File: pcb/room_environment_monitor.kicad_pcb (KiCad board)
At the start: 4 copper layers, 35.5 x 74.7 mm, 54 parts, among them J1 Conn_01x02_Pin, J2 Conn_01x04_Pin, J3 Conn_01x06_Socket, P1 USB_C_Plug_USB2.0, Q1 BSS138, Q3 BSS138, SW1 SW_SPST, U2 ESP32-C3-MINI-1, U3 SGP30-2.5K, U4 BME280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

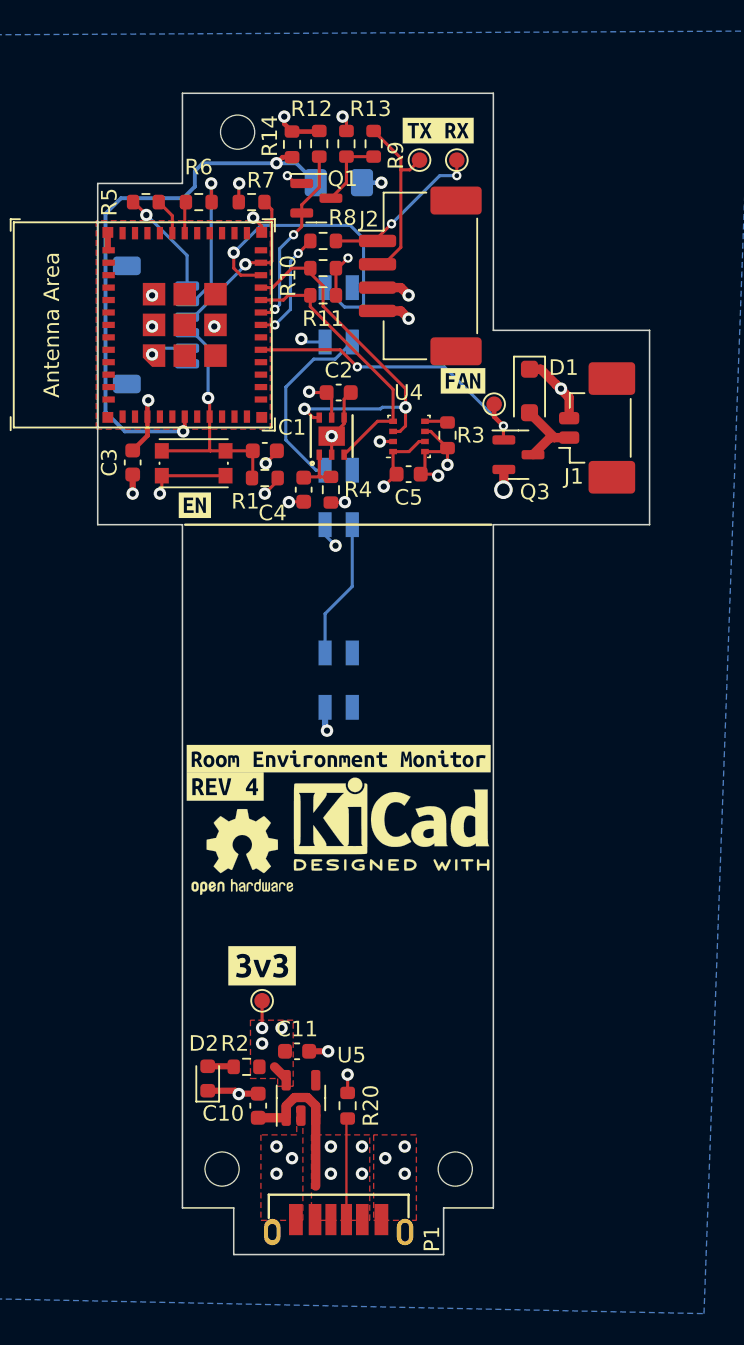
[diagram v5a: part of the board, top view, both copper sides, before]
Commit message: cleanup undeeded pdf files and add gerbers
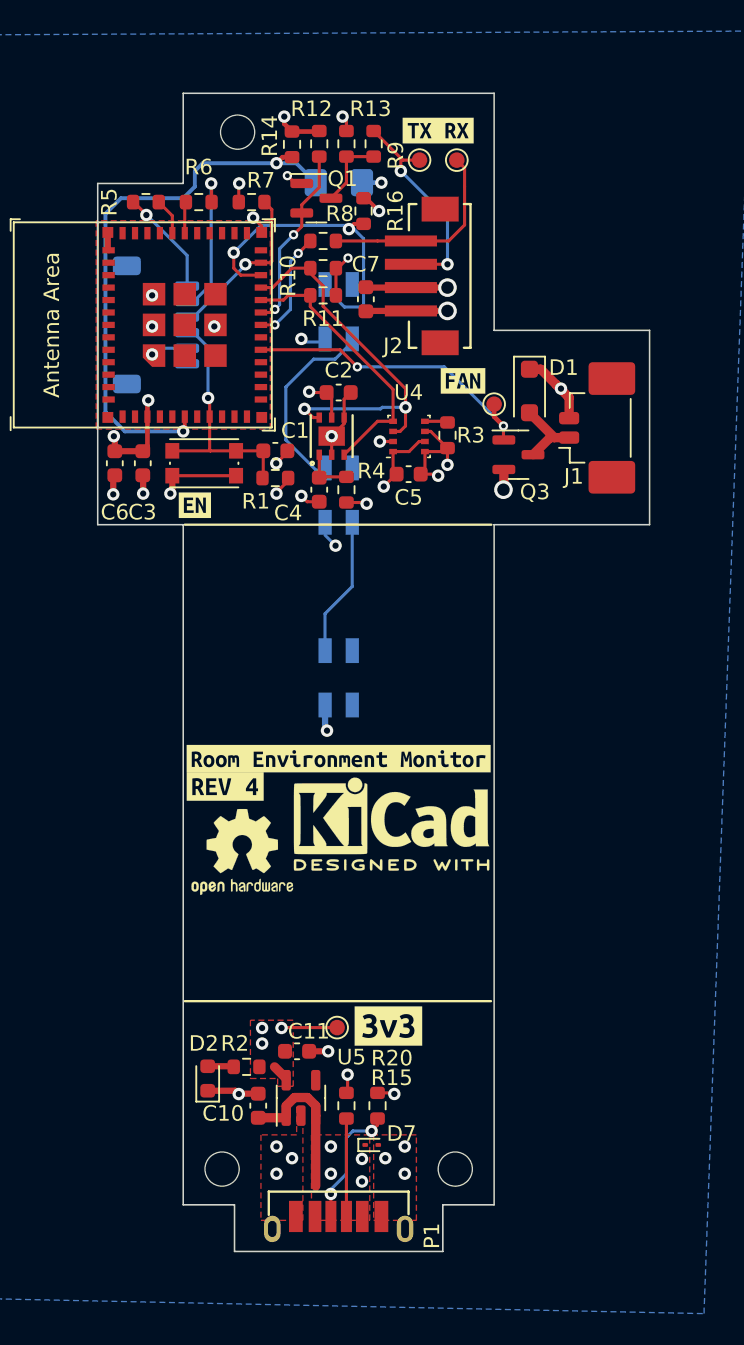
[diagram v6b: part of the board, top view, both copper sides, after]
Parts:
- added C6: 1u, Capacitor_SMD:C_0603_1608Metric, F.Cu at (95.6, 93.8)
- added C7: 1u, Capacitor_SMD:C_0603_1608Metric, F.Cu at (111.8, 83.2)
- added D7: ESD9X3, Diode_SMD:D_SOD-923, F.Cu at (112.1, 137.7)
- added R15: 5.1k, Resistor_SMD:R_0603_1608Metric, F.Cu at (112.5, 135.1)
- added R16: 10k, Resistor_SMD:R_0603_1608Metric, F.Cu at (111.6, 77.6)
- J2: footprint Connector_JST:JST_ZE_BM04B-ZESS-TBT_1x04-1MP_P1.50mm_Vertical -> Kevin_Lutzer_Lbr:CONN_B4B-ZR-SM4-TF_JST
- moved kibuzzard-652F0EDE 9.00 mm to (113.2, 130.0)
- moved TP4 5.12 mm to (109.9, 130.1)
- moved J2 1.25 mm to (116.5, 81.8)
- moved C4 1.00 mm to (108.8, 95.5)
- moved R4 1.00 mm to (110.5, 95.5)
- moved C1 0.67 mm to (105.9, 93.0)
- moved R1 0.67 mm to (105.9, 94.8)
- moved SW1 0.67 mm to (101.3, 93.8)
- moved C3 0.65 mm to (97.4, 93.8)
- moved D3 0.20 mm to (110.0, 84.0)
- moved P1 0.20 mm to (110.0, 143.1)
- moved D4 0.15 mm to (110.0, 95.8)
- moved D5 0.15 mm to (110.0, 107.6)
- moved R20 0.08 mm to (110.5, 135.1)
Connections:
- net CC renamed Net-(P1-CC)
- P1 pad B5: unconnected-(P1-VCONN-PadB5) -> Net-(P1-VCONN)
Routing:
- net Net-(P1-VCONN): track 0.00 -> 8.25 mm, vias 0 -> 2
- net Net-(P1-CC): track 6.53 -> 12.8 mm
- net +3V3: track 26.3 -> 32.4 mm, vias 14 -> 16
- net GND: track 37.1 -> 42.9 mm, vias 26 -> 28
- net +5V: track 17.9 -> 20.9 mm
- net Net-(J2-Pin_2): track 11.1 -> 14.1 mm, vias 0 -> 2
- net Net-(J2-Pin_1): track 10.4 -> 13.1 mm, vias 2 -> 0
- net NEOPIXEL: track 19.7 -> 20.7 mm, vias 1 -> 2
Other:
- board size 35.5 x 74.7 mm -> 35.5 x 74.5 mm

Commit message: update fab
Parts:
- C10: value 10u -> 1u
- C11: value 22u -> 1u
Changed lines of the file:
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@@
         (effects (font (size 1 1) (thickness 0.15)))
     )
-    (fp_text value "22u" (at 0 1.43) (layer "F.Fab")
+    (fp_text value "1u" (at 0 1.43) (layer "F.Fab")
         (effects (font (size 1 1) (thickness 0.15)))
     )
@@
         (effects (font (size 1 1) (thickness 0.15)))
     )
-    (fp_text value "10u" (at 0 1.43 90) (layer "F.Fab") hide
-        (effects (font (size 1 1) (thickness 0.15)))
-    )
+    (fp_text value "1u" (at 0 1.43 90) (layer "F.Fab") hide
+        (effects (font (size 1 1) (thickness 0.15)))
+    )

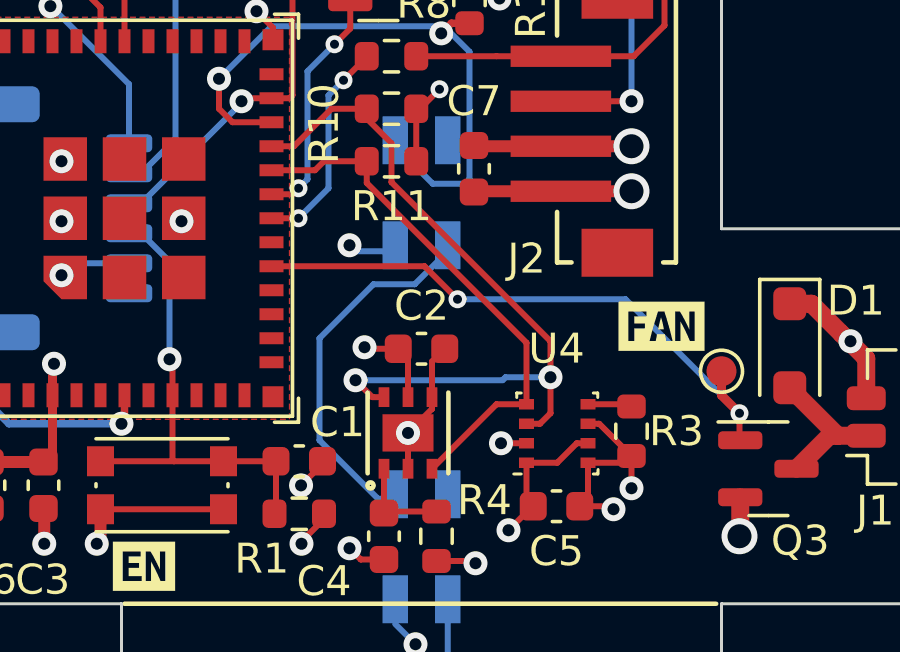
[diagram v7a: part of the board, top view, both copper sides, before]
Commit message: switch the sda and scl lines on the SGP40
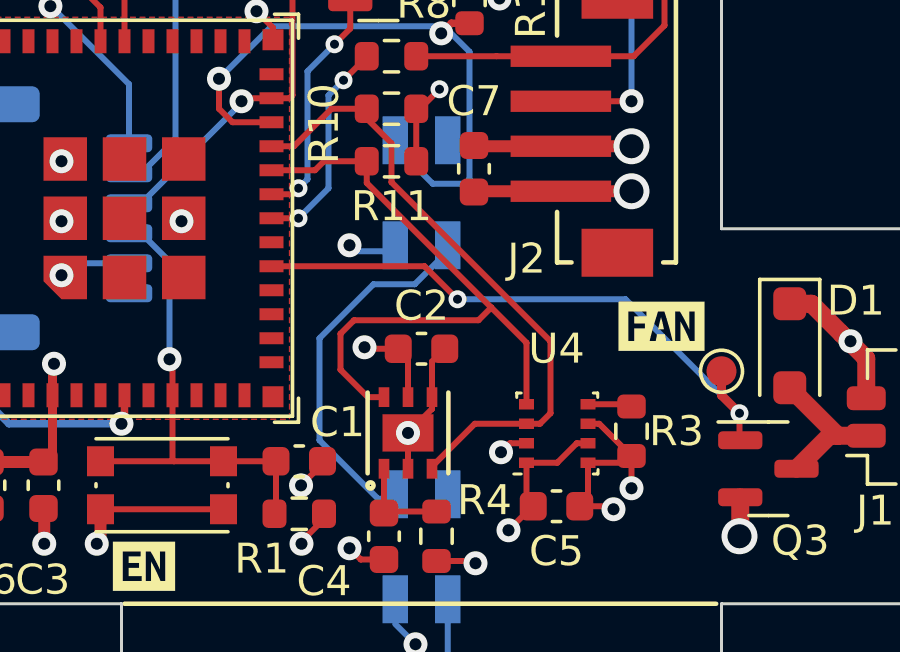
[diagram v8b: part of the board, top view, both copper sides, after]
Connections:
- U3 pad 3: I2C_SCL -> I2C_SDA
- U3 pad 6: I2C_SDA -> I2C_SCL
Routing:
- net I2C_SCL: track 17.6 -> 22.0 mm
- net I2C_SDA: track 24.7 -> 20.8 mm, vias 2 -> 0
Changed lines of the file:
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@@
       (net 2 "GND") (pinfunction "VSS") (pintype "power_in"))
     (pad "3" smd rect (at -1.1938 0.800001 90) (size 0.6604 0.3556) (layers "F.Cu" "F.Paste" "F.Mask")
-      (net 29 "I2C_SCL") (pinfunction "SDA") (pintype "bidirectional"))
+      (net 30 "I2C_SDA") (pinfunction "SDA") (pintype "bidirectional"))
     (pad "4" smd rect (at 1.1938 0.800001 90) (size 0.6604 0.3556) (layers "F.Cu" "F.Paste" "F.Mask")
       (net 2 "GND") (pinfunction "R") (pintype "input"))
@@
       (net 4 "+3V3") (pinfunction "VDDH") (pintype "power_in"))
     (pad "6" smd rect (at 1.1938 -0.800001 90) (size 0.6604 0.3556) (layers "F.Cu" "F.Paste" "F.Mask")
-      (net 30 "I2C_SDA") (pinfunction "SCL") (pintype "input"))
+      (net 29 "I2C_SCL") (pinfunction "SCL") (pintype "input"))
     (pad "7" smd rect (at 0 0 90) (size 1.2446 1.7018) (layers "F.Cu" "F.Paste" "F.Mask")
       (net 2 "GND") (pinfunction "PAD") (pintype "power_in"))
@@
   (segment (start 100.661396 84.4) (end 104 81.061396) (width 0.2) (layer "B.Cu") (net 3))
   (segment (start 115.55 93.05) (end 115.55 94.225) (width 0.2) (layer "F.Cu") (net 4))
+  (segment (start 113.5 92.4) (end 112.95 92.4) (width 0.2) (layer "F.Cu") (net 4))
   (segment (start 103.575 77) (end 103.575 75.825) (width 0.2) (layer "F.Cu") (net 4))
   (segment (start 106.5 71.9625) (end 107 72.4625) (width 0.3) (layer "F.Cu") (net 4))
@@
   (segment (start 103.575 75.825) (end 103.6 75.8) (width 0.2) (layer "F.Cu") (net 4))
   (segment (start 97.425 92.975) (end 97.7 92.7) (width 0.3) (layer "F.Cu") (net 4))
-  (segment (start 113.5 92.4) (end 112.6495 92.4) (width 0.2) (layer "F.Cu") (net 4))
+  (segment (start 112.95 92.4) (end 112.65 92.7) (width 0.2) (layer "F.Cu") (net 4))
   (segment (start 109.95 81.25) (end 110.6 80.6) (width 0.2) (layer "F.Cu") (net 4))
   (segment (start 106.625 133.375) (end 105.875 132.625) (width 0.6) (layer "F.Cu") (net 4))
@@
   (via (at 105.075 130.125) (size 0.8) (drill 0.4) (layers "F.Cu" "B.Cu") (free) (net 4))
   (via (at 95.537701 92.062299) (size 0.8) (drill 0.4) (layers "F.Cu" "B.Cu") (net 4))
-  (via (at 112.6495 92.4) (size 0.8) (drill 0.4) (layers "F.Cu" "B.Cu") (net 4))
+  (via (at 112.65 92.7) (size 0.8) (drill 0.4) (layers "F.Cu" "B.Cu") (net 4))
   (via (at 105.075 131.125) (size 0.8) (drill 0.4) (layers "F.Cu" "B.Cu") (free) (net 4))
   (via (at 106.325 130.125) (size 0.8) (drill 0.4) (layers "F.Cu" "B.Cu") (free) (net 4))
@@
   (segment (start 110.499999 142.450002) (end 110.499999 136.025001) (width 0.15) (layer "F.Cu") (net 19))
   (segment (start 110.5 135.95) (end 110.499999 142.250002) (width 0.2) (layer "F.Cu") (net 19))
-  (segment (start 112.500002 91.1) (end 113.5 91.1) (width 0.2) (layer "F.Cu") (net 29))
-  (segment (start 110.350002 93.25) (end 112.500002 91.1) (width 0.2) (layer "F.Cu") (net 29))
+  (segment (start 108.75 90.8624) (end 108.2124 90.8624) (width 0.2) (layer "F.Cu") (net 29))
+  (segment (start 107.75 88.3) (end 111.9 88.3) (width 0.2) (layer "F.Cu") (net 29))
+  (segment (start 108.2124 90.8624) (end 107.3 89.95) (width 0.2) (layer "F.Cu") (net 29))
+  (segment (start 107.3 89.95) (end 107.3 88.75) (width 0.2) (layer "F.Cu") (net 29))
   (segment (start 106.45 83.3) (end 106.75 83) (width 0.2) (layer "F.Cu") (net 29))
+  (segment (start 112.325 87.875) (end 108.175 83.725) (width 0.2) (layer "F.Cu") (net 29))
   (segment (start 106.75 83) (end 108.175 83) (width 0.2) (layer "F.Cu") (net 29))
+  (segment (start 107.3 88.75) (end 107.75 88.3) (width 0.2) (layer "F.Cu") (net 29))
+  (segment (start 113.5 89.05) (end 112.325 87.875) (width 0.2) (layer "F.Cu") (net 29))
   (segment (start 113.5 91.1) (end 113.5 89.05) (width 0.2) (layer "F.Cu") (net 29))
   (segment (start 105 83.3) (end 106.45 83.3) (width 0.2) (layer "F.Cu") (net 29))
-  (segment (start 113.5 89.05) (end 108.175 83.725) (width 0.2) (layer "F.Cu") (net 29))
+  (segment (start 111.9 88.3) (end 112.325 87.875) (width 0.2) (layer "F.Cu") (net 29))
   (segment (start 108.175 83.725) (end 108.175 83) (width 0.2) (layer "F.Cu") (net 29))
+  (segment (start 111.777801 91.75) (end 110.350002 93.177799) (width 0.2) (layer "F.Cu") (net 30))
   (segment (start 114.3 91.4) (end 113.95 91.75) (width 0.2) (layer "F.Cu") (net 30))
-  (segment (start 108.3624 90.8624) (end 107.8 90.3) (width 0.2) (layer "F.Cu") (net 30))
+  (segment (start 110.350002 93.177799) (end 110.350002 93.25) (width 0.2) (layer "F.Cu") (net 30))
   (segment (start 105.75 82.5) (end 107 81.25) (width 0.2) (layer "F.Cu") (net 30))
   (segment (start 109 83.7) (end 114.3 89) (width 0.2) (layer "F.Cu") (net 30))
   (segment (start 105 82.5) (end 105.75 82.5) (width 0.2) (layer "F.Cu") (net 30))
   (segment (start 109 82.4) (end 109 83.7) (width 0.2) (layer "F.Cu") (net 30))
+  (segment (start 113.5 91.75) (end 111.777801 91.75) (width 0.2) (layer "F.Cu") (net 30))
   (segment (start 113.95 91.75) (end 113.5 91.75) (width 0.2) (layer "F.Cu") (net 30))
   (segment (start 108.175 81.575) (end 109 82.4) (width 0.2) (layer "F.Cu") (net 30))
   (segment (start 114.3 89) (end 114.3 91.4) (width 0.2) (layer "F.Cu") (net 30))
   (segment (start 107 81.25) (end 108.175 81.25) (width 0.2) (layer "F.Cu") (net 30))
-  (segment (start 108.75 90.8624) (end 108.3624 90.8624) (width 0.2) (layer "F.Cu") (net 30))
-  (via (at 107.8 90.3) (size 0.8) (drill 0.4) (layers "F.Cu" "B.Cu") (net 30))
-  (via (at 114.3 90.2) (size 0.8) (drill 0.4) (layers "F.Cu" "B.Cu") (net 30))
-  (segment (start 112.7005 90.3) (end 112.8005 90.2) (width 0.2) (layer "B.Cu") (net 30))
-  (segment (start 107.8 90.3) (end 112.7005 90.3) (width 0.2) (layer "B.Cu") (net 30))
-  (segment (start 112.8005 90.2) (end 114.3 90.2) (width 0.2) (layer "B.Cu") (net 30))
   (segment (start 109.500001 142.250002) (end 109.5 140.8) (width 0.2) (layer "F.Cu") (net 41))
   (segment (start 112.5 135.95) (end 112.5 136.37) (width 0.2) (layer "F.Cu") (net 41))
